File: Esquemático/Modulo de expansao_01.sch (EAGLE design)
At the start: 96 parts, among them IC1 MCP25050-I/P, IC2 MCP2551-I/P, IC3 LM1117T-3.3/NOPB, K1 AQYAQY27, K2 AQYAQY27, K3 AQYAQY27, K4 AQYAQY27, K5 AQYAQY27, K6 AQYAQY27, Q2 20M, T1 2N3904, T2 2N3904, T3 2N3904, T4 2N3904, T5 2N3904, T6 2N3904, T7 2N3904, T8 2N3904

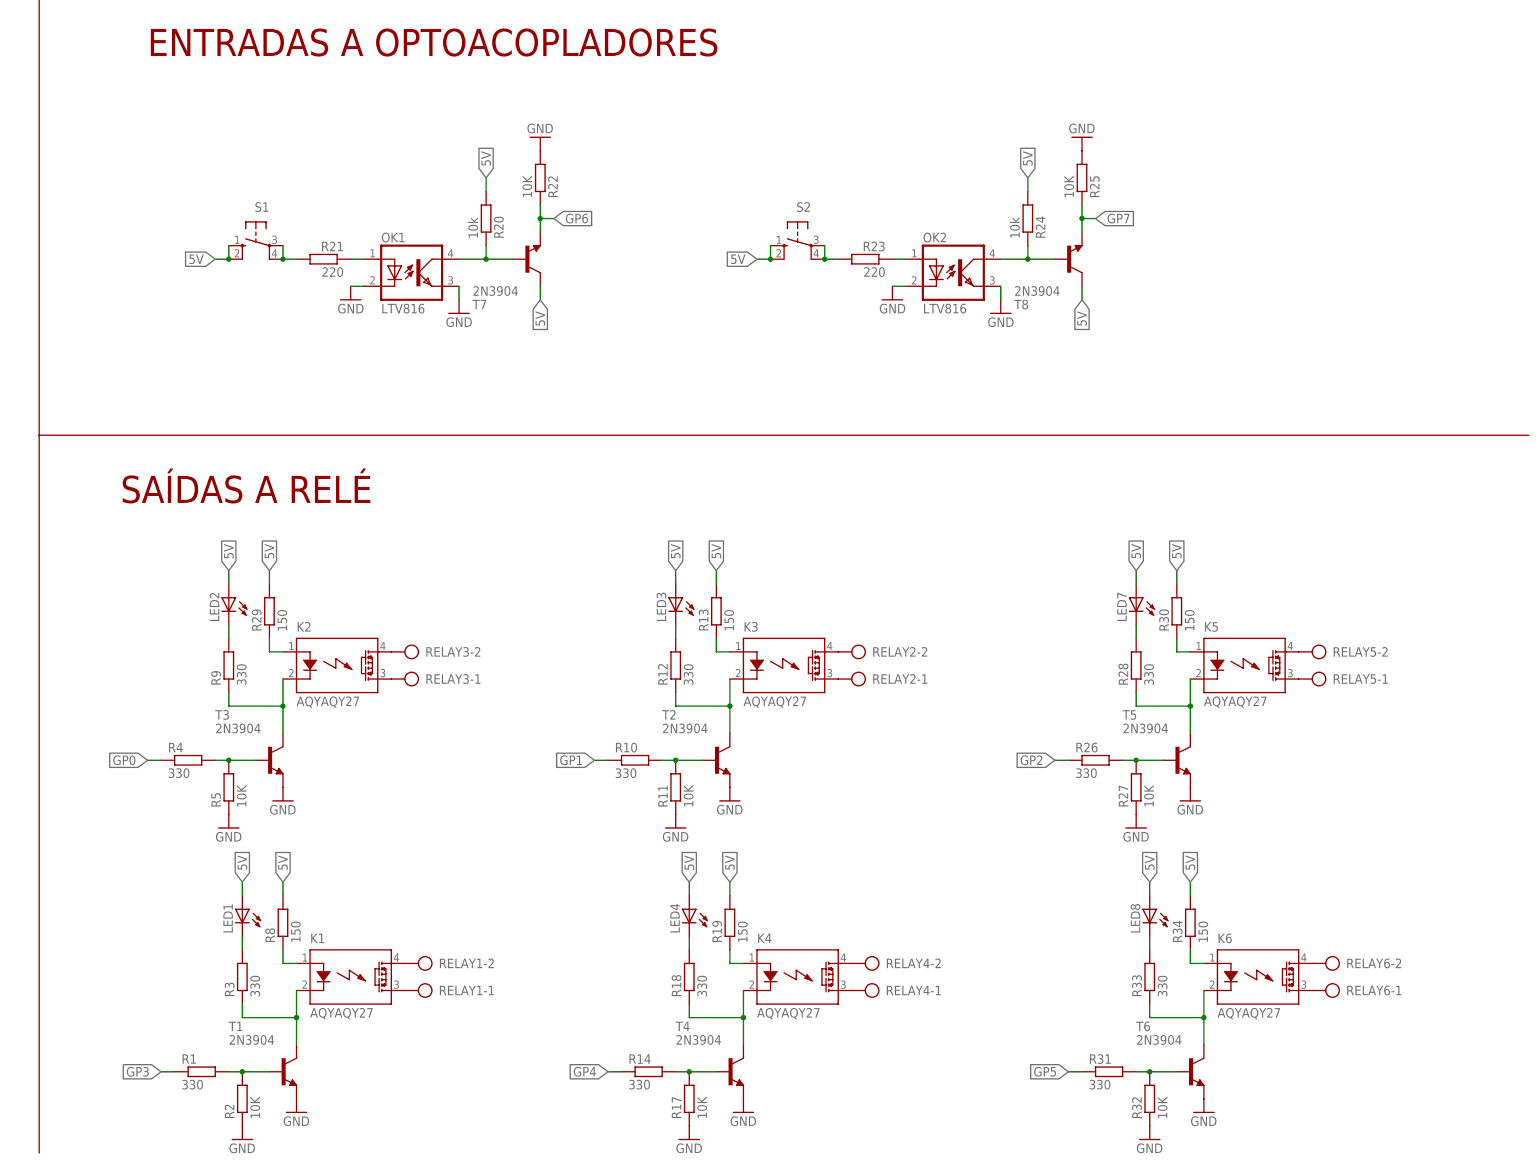
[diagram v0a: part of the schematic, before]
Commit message: Entradas e saidas testadas no modulo de expansao.
Falta somente testar as ligaçoes no que se refere à comunicação
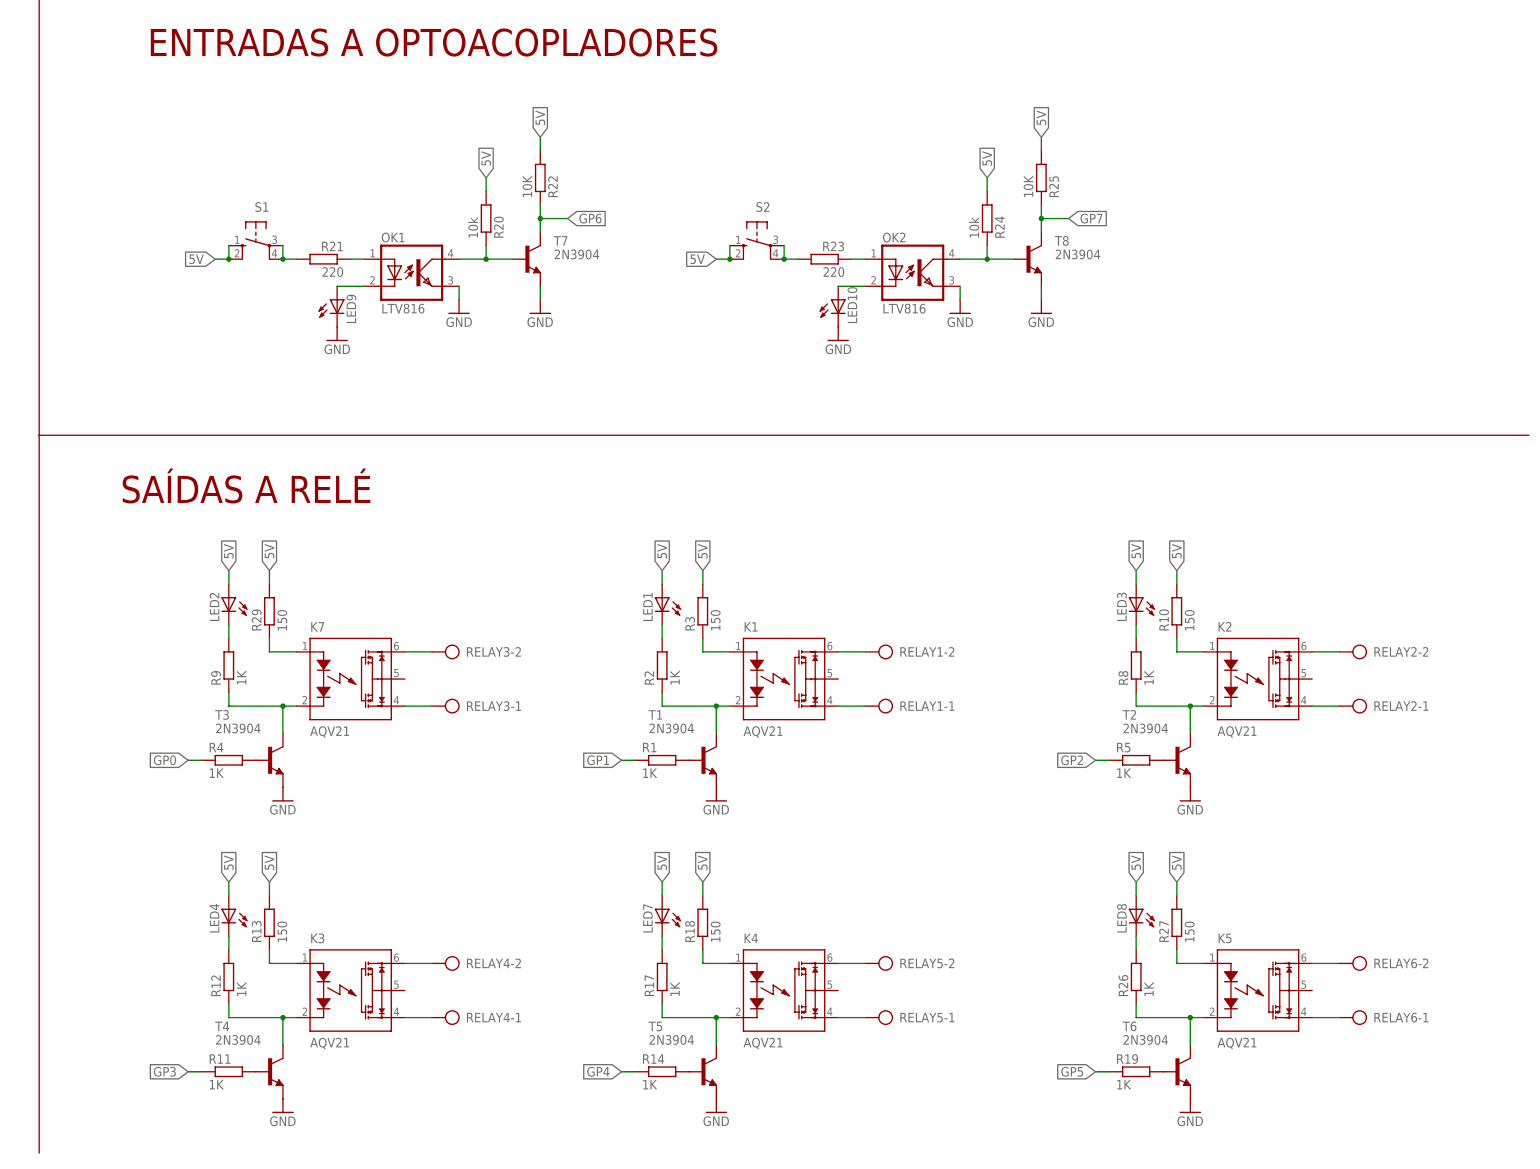
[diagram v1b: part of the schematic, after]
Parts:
- removed K6: AQYAQY27, relay:AQYAQY27
- removed R28, R31, R33: 330, rcl:R-EU_0204/5
- removed R30, R34: 150, rcl:R-EU_0204/5
- removed R32: 10K, rcl:R-EU_0204/5
- added K7: AQV21, relay:AQV21
- added LED10, LED9: (no value), led:LED3MM
- K1, K2, K3, K4, K5: value AQYAQY27 -> AQV21; device relay:AQYAQY27 -> relay:AQV21
- R1, R12, R14, R26, R4, R9: value 330 -> 1K
- R10, R18, R3: value 330 -> 150
- R11, R17, R2, R5: value 10K -> 1K
- R19, R8: value 150 -> 1K
- R27: value 10K -> 150
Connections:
- new net N$41: LED9.A, OK1.C
- new net N$42: LED10.A, OK2.C
- net 5V: now also K7.A, R10.1, R10.2, R18.1, R18.2, R22.2, R25.2, R27.1, R27.2, R3.1, R3.2; no longer K6.A, R19.1, R19.2, R30.1, R30.2, R34.1, R34.2, R8.1, R8.2, T7.C, T8.C
- net GND: now also LED10.C, LED9.C, T7.E, T8.E; no longer OK1.C, OK2.C, R11.1, R17.1, R2.1, R22.2, R25.2, R27.1, R32.1, R5.1
- net GP1: now also R1.1; no longer R10.1
- net GP2: now also R5.1; no longer R26.1
- net GP3: now also R11.1; no longer R1.1
- net GP5: now also R19.1; no longer R31.1
- net GP6: now also T7.C; no longer T7.E
- net GP7: now also T8.C; no longer T8.E
- net N$1: now also R2.2; no longer R3.2
- net N$10: no longer R5.2
- net N$12: now also K7.K; no longer K2.K
- net N$13: now also K7.D1, RELAY3-2.KL; no longer K2.DS2, RELAY3-1.KL
- net N$14: now also K7.D2, RELAY3-1.KL; no longer K2.DS1, RELAY3-2.KL
- net N$15: now also K2.D2, RELAY2-1.KL; no longer K3.DS1, RELAY2-2.KL
- net N$16: now also R12.2; no longer R18.2
- net N$17: now also K3.K, R12.1; no longer K4.K, R18.1
- net N$18: now also R11.2; no longer R14.2, R17.2
- net N$19: now also K3.D1, RELAY4-2.KL; no longer K4.DS2, RELAY4-1.KL
- net N$2: now also R2.1; no longer R3.1
- net N$20: now also K3.D2, RELAY4-1.KL; no longer K4.DS1, RELAY4-2.KL
- net N$22: now also R17.2; no longer R28.2
- net N$26: now also K4.K, R17.1; no longer K5.K, R28.1
- net N$27: now also R14.2; no longer R26.2, R27.2
- net N$28: now also K4.D1, RELAY5-2.KL; no longer K5.DS2, RELAY5-1.KL
- net N$29: now also K4.D2, RELAY5-1.KL; no longer K5.DS1, RELAY5-2.KL
- net N$3: no longer R2.2
- net N$30: now also R26.2; no longer R33.2
- net N$33: now also K5.K, R26.1; no longer K6.K, R33.1
- net N$34: now also R19.2; no longer R31.2, R32.2
- net N$35: now also K5.D1, RELAY6-2.KL; no longer K6.DS2, RELAY6-1.KL
- net N$36: now also K5.D2, RELAY6-1.KL; no longer K6.DS1, RELAY6-2.KL
- net N$4: now also K1.D1, RELAY1-2.KL; no longer K1.DS2, RELAY1-1.KL
- net N$5: now also K1.D2, RELAY1-1.KL; no longer K1.DS1, RELAY1-2.KL
- net N$6: now also R8.2; no longer R12.2
- net N$7: now also K2.K, R8.1; no longer K3.K, R12.1
- net N$8: now also R5.2; no longer R10.2, R11.2
- net N$9: now also K2.D1, RELAY2-2.KL; no longer K3.DS2, RELAY2-1.KL
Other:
- moved on the sheet: LED1, LED3, LED4, LED7, LED8, OK2, R1, R10, R11, R12, R13, R14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

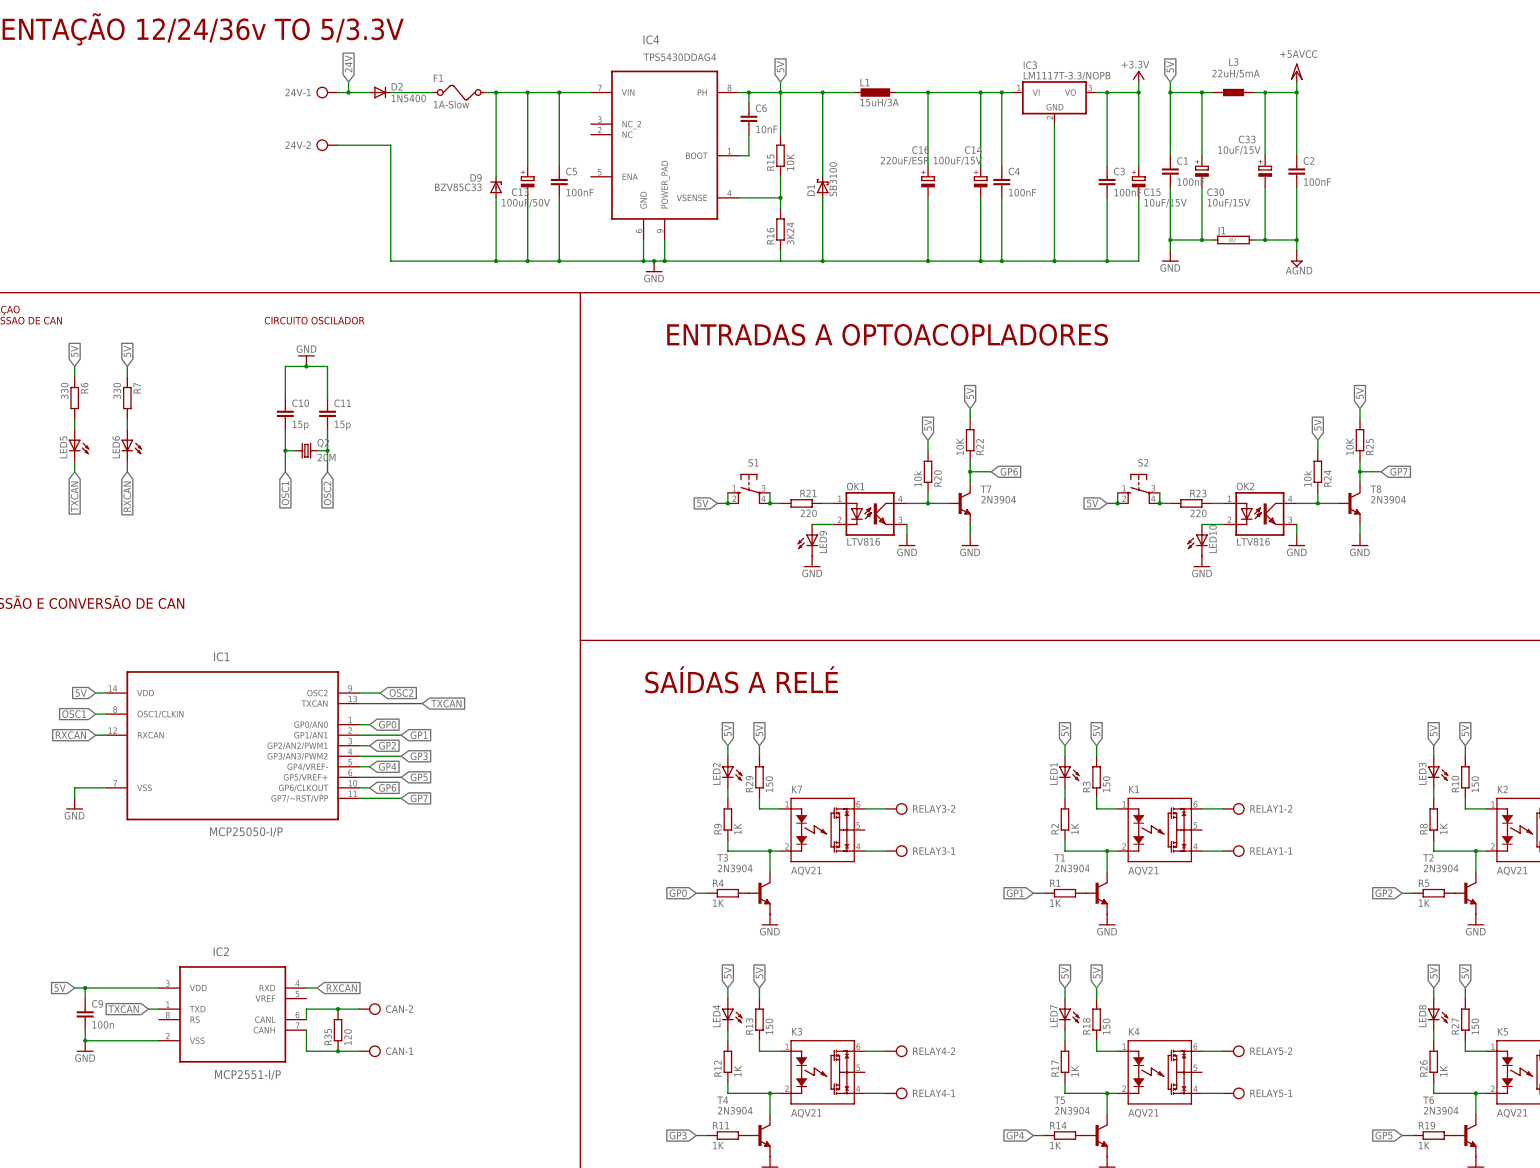
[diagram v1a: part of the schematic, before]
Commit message: actualizaçao esquematico e brd do modulo expansao
versoes finais do modulo espansao, do esquematico e board
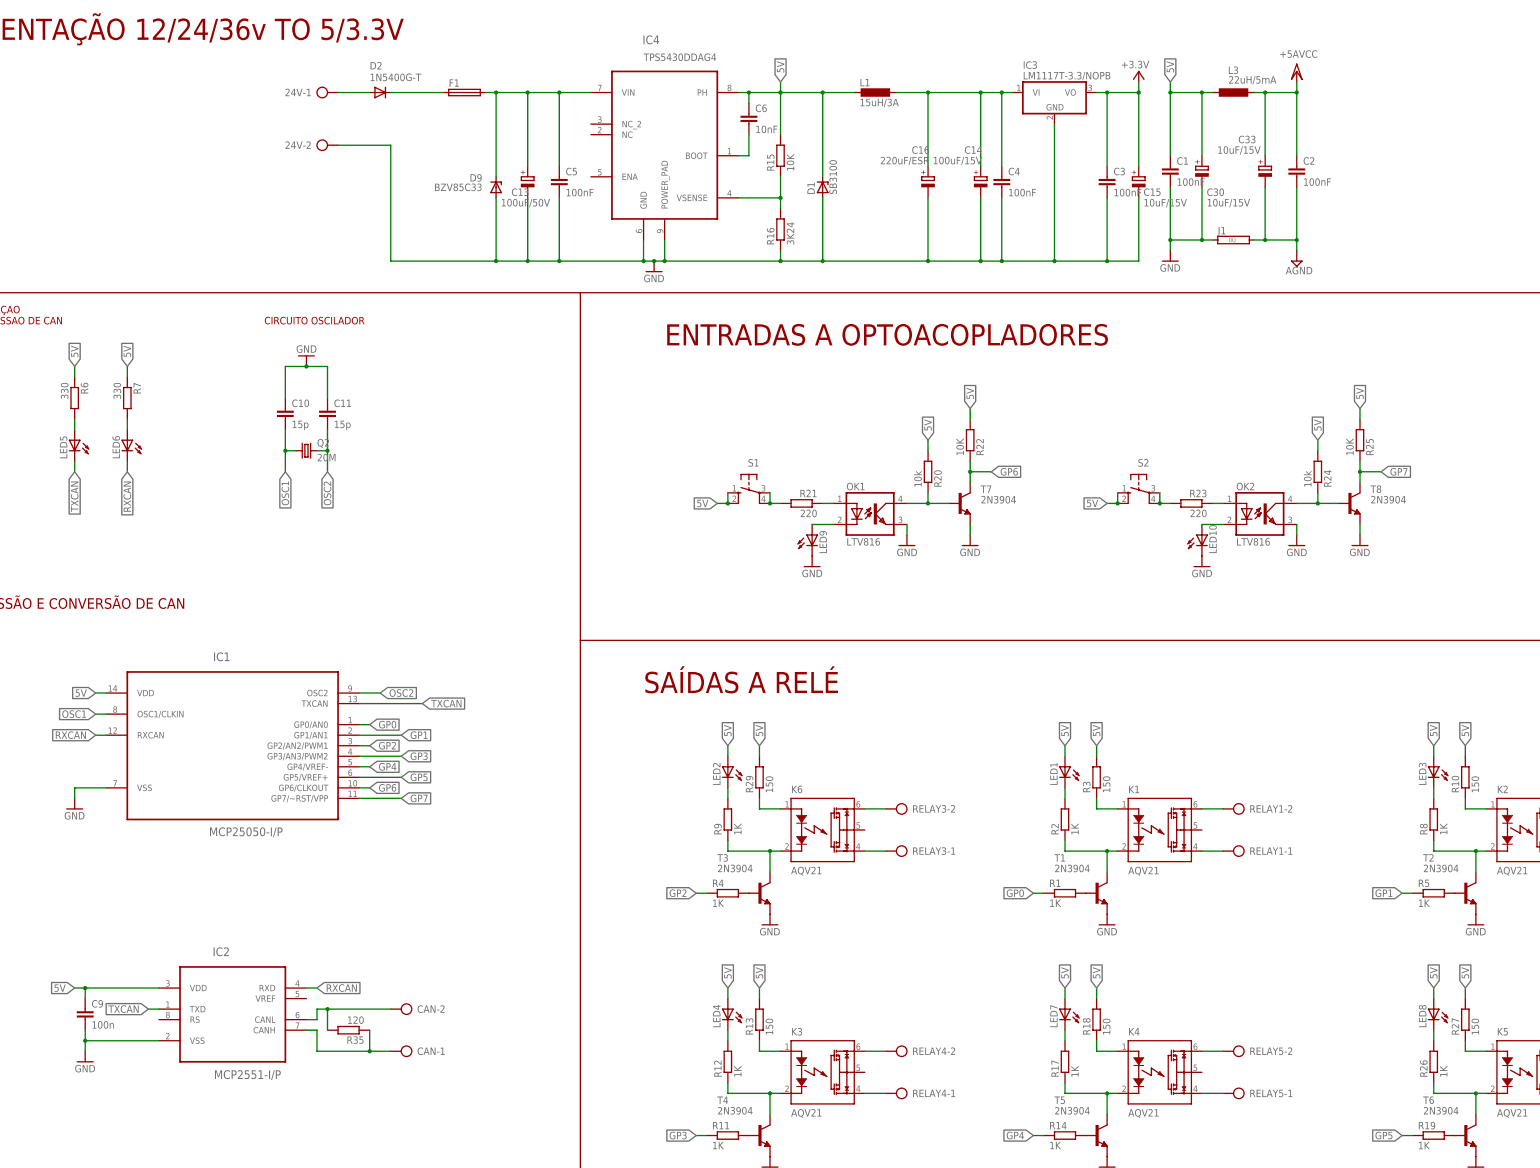
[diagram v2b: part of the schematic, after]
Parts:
- C13: device rcl:CPOL-EUE5-10.5 -> rcl:CPOL-EUE3.5-10
- C14, C15: device rcl:CPOL-EUE5-10.5 -> rcl:CPOL-EUE2-5
- C16: device rcl:CPOL-EUE5-10.5 -> rcl:CPOL-EUE2.5-7
- C30, C33: device rcl:CPOL-EUE5-10.5 -> rcl:CPOL-EUE2.5-6
- C6: device rcl:C-EU075-032X103 -> rcl:C-EU025-025X050
- C9: device rcl:C-EU050-025X075 -> rcl:C-EU050-024X044
- D1: device diode:1N5908 -> diode:BZV10
- D2: value 1N5400 -> 1N5400G-T; device diode:1N5400 -> diode:AA112
- D9: device diode:ZENER-DIODEF126-10 -> diode:BZV10
- F1: value 1A-Slow -> (none); device special:FUSE -> fuse:TR5
- L1: device rcl:L-EUTJ3-U1 -> rcl:L-EU6000-XXX-RC
- L3: device inductors:BL01RN1A -> rcl:L-EU6000-XXX-RC
- R1, R10, R11, R12, R13, R14, R17, R18, R19, R2, R20, R21, R22, R23, R24, R25, R26, R27, R29, R3, R35, R4, R5, R6, R7, R8, R9: device rcl:R-EU_0204/5 -> rcl:R-EU_0207/10
- R15, R16: device rcl:R-EU_0204/7 -> rcl:R-EU_0207/10
- renumbered K7 to K6
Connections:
- new net N$43: K2.A, R10.1
- new net N$44: K4.A, R18.1
- new net N$45: K1.A, R3.1
- new net N$46: K3.A, R13.1
- new net N$47: K5.A, R27.1
- new net N$48: K6.A, R29.1
- net 5V: no longer K1.A, K2.A, K3.A, K4.A, K5.A, K6.A, R10.1, R13.1, R18.1, R27.1, R29.1, R3.1
- net GP0: now also R1.1; no longer R4.1
- net GP1: now also R5.1; no longer R1.1
- net GP2: now also R4.1; no longer R5.1
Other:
- moved on the sheet: CAN-1, CAN-2, L3, R35
